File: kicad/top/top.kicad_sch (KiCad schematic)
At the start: 32 parts, among them J1 OLED_128x64, J2 Conn_01x15, SW1 SW_SPDT, SW2 RotaryEncoder_Switch

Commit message: added bottom part of pcb, added 3d model for adafruit feather v2
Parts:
- removed H1, H2, H3, H4: MountingHole, MountingHole:MountingHole_2.2mm_M2, symbol Mechanical:MountingHole
- added H1, H2, H3, H4: MountingHole_Pad, MountingHole:MountingHole_2.2mm_M2_DIN965_Pad, symbol Mechanical:MountingHole_Pad
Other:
- note added: "Top Board"

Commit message: on bottom pcb moved signal connections from back copper to front, left most back copper as ground plane. aligned pins and pin sockets on top and bottom pcb, centered them.
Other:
- note added: "62 mm board 35.5 mm pins"
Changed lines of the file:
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@@
+		)
+	)
+	(text "62 mm board\n35.5 mm pins"
+		(exclude_from_sim no)
+		(at 218.44 110.236 0)
+		(effects
+			(font
+				(size 1.27 1.27)
+			)
 		)
 	)

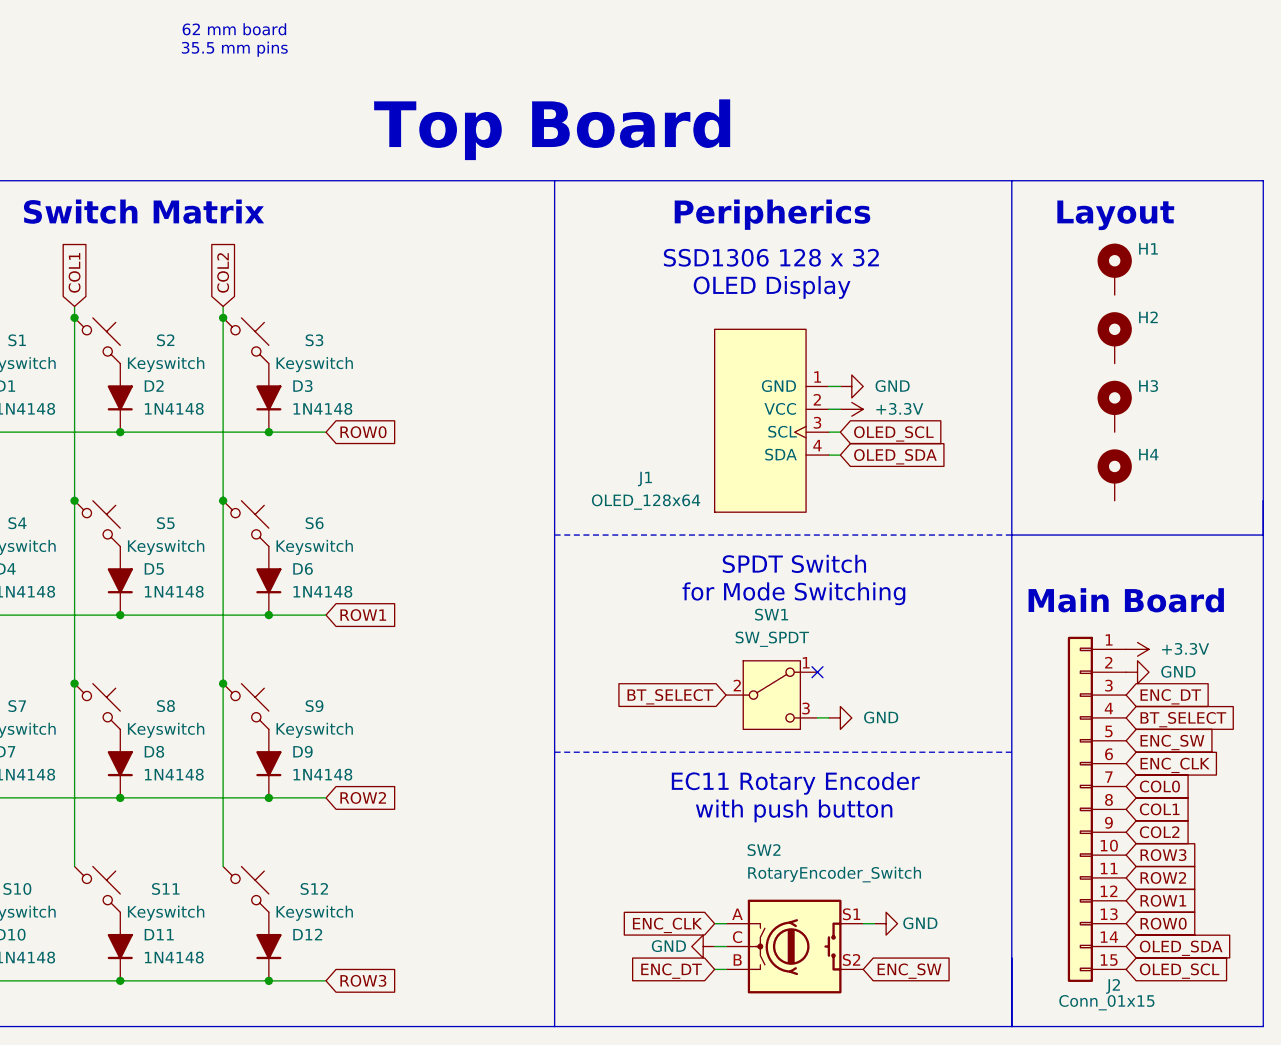
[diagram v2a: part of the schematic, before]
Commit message: modify paths and file locations for portability, added mounting pins to encoder, changed symbol, footprint and 3d of switch to correlate to what im using
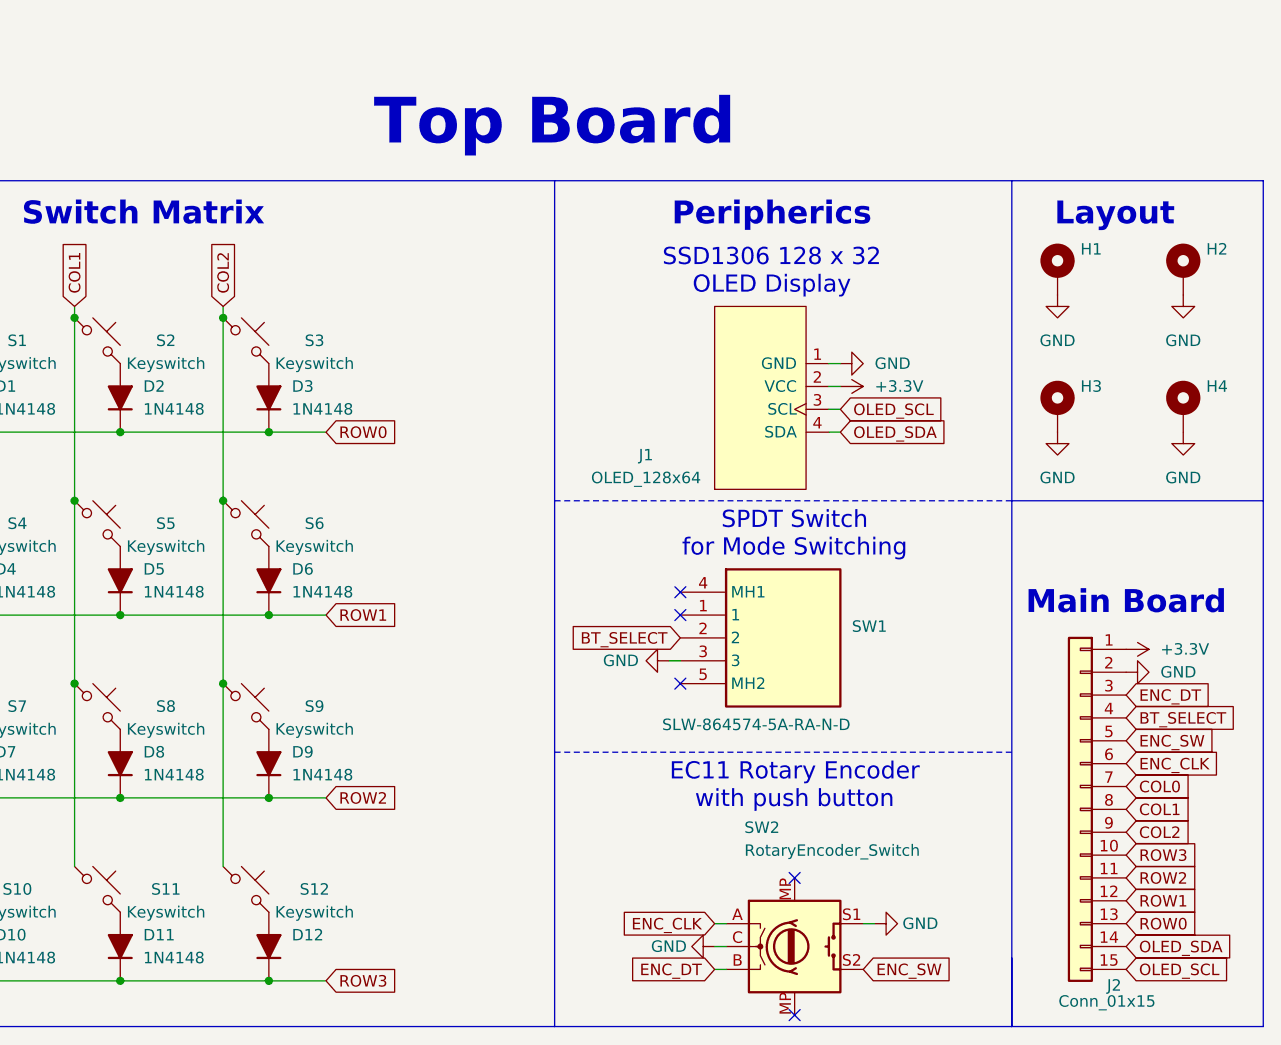
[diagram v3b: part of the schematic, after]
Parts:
- removed SW1: SW_SPDT, Button_Switch_THT:SW_Slide_SPDT_Angled_CK_OS102011MA1Q, symbol Switch:SW_SPDT
- added SW1: SLW-864574-5A-RA-N-D, Project-Footprints:SLW8645745ARAND, symbol Top-Library:SLW-864574-5A-RA-N-D
- D1, D10, D11, D12, D2, D3, D4, D5, D6, D7, D8, D9: footprint Diode_THT:D_DO-35_SOD27_P7.62mm_Horizontal -> Project-Footprints:D_DO-35_SOD27_P7.62mm_Horizontal; symbol PCM_Diode_AKL:1N4148 -> Top-Library:1N4148
- H1, H2, H3, H4: footprint MountingHole:MountingHole_2.2mm_M2_DIN965_Pad -> Project-Footprints:MountingHole_2.2mm_M2_DIN965_Pad; symbol Mechanical:MountingHole_Pad -> Top-Library:MountingHole_Pad
- J1: footprint ScottoKeebs_Components:OLED_128x64 -> Project-Footprints:OLED_128x64; symbol ScottoKeebs:OLED_128x64 -> Top-Library:OLED_128x64
- J2: footprint Connector_PinHeader_2.54mm:PinHeader_1x15_P2.54mm_Vertical -> Project-Footprints:PinHeader_1x15_P2.54mm_Vertical; symbol Connector_Generic:Conn_01x15 -> Top-Library:Conn_01x15
- S1, S10, S11, S12, S2, S3, S4, S5, S6, S7, S8, S9: footprint ScottoKeebs_Scotto:MX_Hotswap_1.00u -> Project-Footprints:MX_Hotswap_1.00u; symbol ScottoKeebs:Placeholder_Keyswitch -> Top-Library:Placeholder_Keyswitch
- SW2: footprint ScottoKeebs_Scotto:Encoder_EC11_MX -> Project-Footprints:Encoder_EC11_MX; symbol Device:RotaryEncoder_Switch -> Top-Library:RotaryEncoder_Switch
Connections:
- net BT_SELECT: now also SW1.2
- net GND: now also H1.1, H2.1, H3.1, H4.1, SW1.3
- no-connect marks 1 -> 5
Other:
- note removed: "62 mm board 35.5 mm pins"
- moved on the sheet: H1, H2, H3, H4, J1

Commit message: finalised mounting hole and pins position, changed gpios
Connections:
- net +3.3V: now also SW1.1
- net COL0: now also J2.11 (Pin_11); no longer J2.7 (Pin_7)
- net COL1: now also J2.12 (Pin_12); no longer J2.8 (Pin_8)
- net COL2: now also J2.13 (Pin_13); no longer J2.9 (Pin_9)
- net ENC_CLK: now also J2.8 (Pin_8); no longer J2.6 (Pin_6)
- net ENC_DT: now also J2.9 (Pin_9); no longer J2.3 (Pin_3)
- net ENC_SW: now also J2.10 (Pin_10); no longer J2.5 (Pin_5)
- net GND: now also SW1.4 (MH1), SW1.5 (MH2), SW2.MP
- net OLED_SCL: now also J2.14 (Pin_14); no longer J2.15 (Pin_15)
- net OLED_SDA: now also J2.15 (Pin_15); no longer J2.14 (Pin_14)
- net ROW0: now also J2.7 (Pin_7); no longer J2.13 (Pin_13)
- net ROW1: now also J2.6 (Pin_6); no longer J2.12 (Pin_12)
- net ROW2: now also J2.5 (Pin_5); no longer J2.11 (Pin_11)
- net ROW3: now also J2.3 (Pin_3); no longer J2.10 (Pin_10)
- no-connect marks 5 -> 0
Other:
- moved on the sheet: D1, D10, D11, D12, D2, D3, D4, D5, D6, D7, D8, D9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

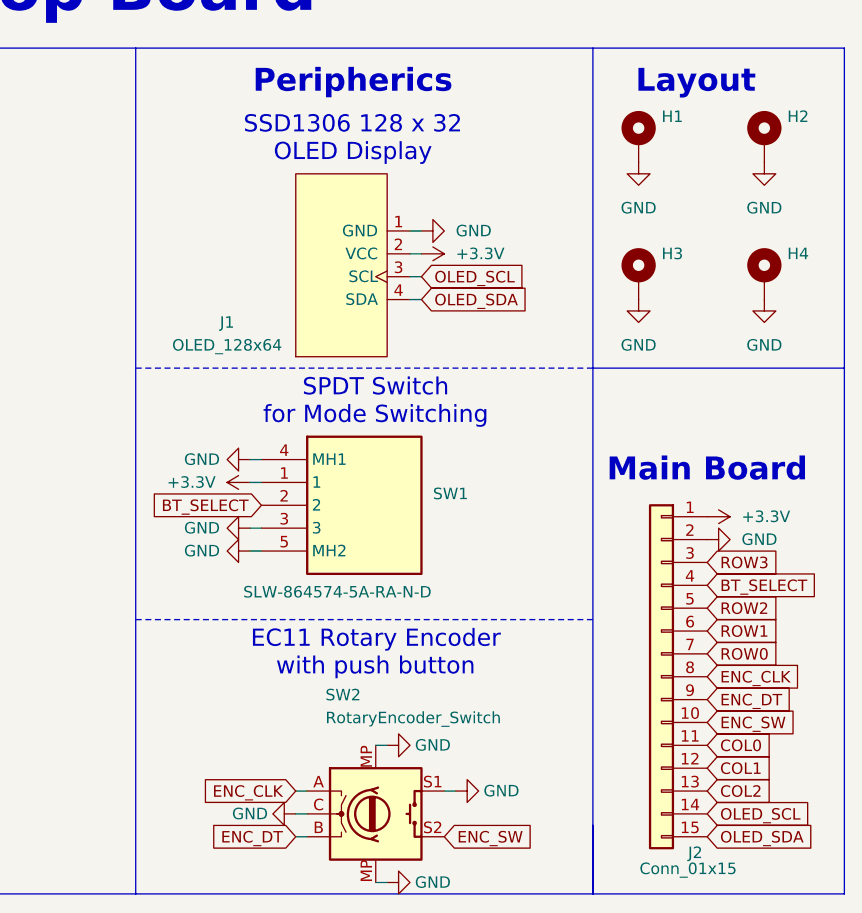
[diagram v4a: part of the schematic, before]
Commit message: Changed from Adafruit Feather V2 to UnkownMaker ProS3 [D] for USB HID feature. Changed OLED from 128x64 to 128x32
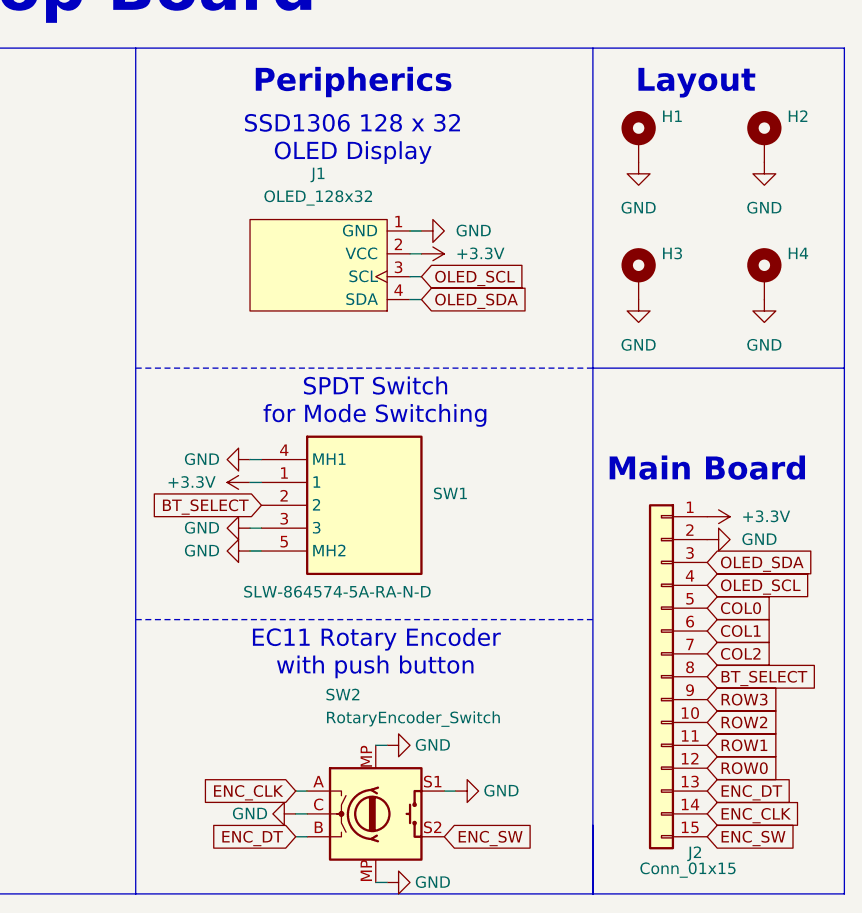
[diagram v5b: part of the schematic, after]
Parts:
- removed J1: OLED_128x64, Project-Footprints:OLED_128x64, symbol Top-Library:OLED_128x64
- added J1: OLED_128x32, ScottoKeebs_Components:OLED_128x32, symbol ScottoKeebs:OLED_128x32
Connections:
- net +3.3V: now also J1.2 (VCC)
- net BT_SELECT: now also J2.8 (Pin_8); no longer J2.4 (Pin_4)
- net COL0: now also J2.5 (Pin_5); no longer J2.11 (Pin_11)
- net COL1: now also J2.6 (Pin_6); no longer J2.12 (Pin_12)
- net COL2: now also J2.7 (Pin_7); no longer J2.13 (Pin_13)
- net ENC_CLK: now also J2.14 (Pin_14); no longer J2.8 (Pin_8)
- net ENC_DT: now also J2.13 (Pin_13); no longer J2.9 (Pin_9)
- net ENC_SW: now also J2.15 (Pin_15); no longer J2.10 (Pin_10)
- net GND: now also J1.1 (GND)
- net OLED_SCL: now also J2.4 (Pin_4), J1.3 (SCL); no longer J2.14 (Pin_14)
- net OLED_SDA: now also J2.3 (Pin_3), J1.4 (SDA); no longer J2.15 (Pin_15)
- net ROW0: now also J2.12 (Pin_12); no longer J2.7 (Pin_7)
- net ROW1: now also J2.11 (Pin_11); no longer J2.6 (Pin_6)
- net ROW2: now also J2.10 (Pin_10); no longer J2.5 (Pin_5)
- net ROW3: now also J2.9 (Pin_9); no longer J2.3 (Pin_3)
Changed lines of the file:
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@@
 	(global_label "ROW0"
 		(shape input)
-		(at 208.28 109.22 0)
+		(at 208.28 121.92 0)
 		(fields_autoplaced yes)
 		(effects
@@
 		)
 		(property "Intersheetrefs" "${INTERSHEET_REFS}"
-			(at 216.5266 109.22 0)
+			(at 216.5266 121.92 0)
 			(effects
 				(font
@@
 	(global_label "OLED_SDA"
 		(shape input)
-		(at 208.28 129.54 0)
+		(at 208.28 99.06 0)
 		(fields_autoplaced yes)
 		(effects
@@
 		)
 		(property "Intersheetrefs" "${INTERSHEET_REFS}"
-			(at 220.5785 129.54 0)
+			(at 220.5785 99.06 0)
 			(effects
 				(font
@@
 	(global_label "ENC_DT"
 		(shape input)
-		(at 208.28 114.3 0)
+		(at 208.28 124.46 0)
 		(fields_autoplaced yes)
 		(effects
@@
 		)
 		(property "Intersheetrefs" "${INTERSHEET_REFS}"
-			(at 218.2199 114.3 0)
+			(at 218.2199 124.46 0)
 			(effects
 				(font
@@
 	(global_label "COL0"
 		(shape input)
-		(at 208.28 119.38 0)
+		(at 208.28 104.14 0)
 		(fields_autoplaced yes)
 		(effects
@@
 		)
 		(property "Intersheetrefs" "${INTERSHEET_REFS}"
-			(at 216.1033 119.38 0)
+			(at 216.1033 104.14 0)
 			(effects
 				(font
@@
 	(global_label "BT_SELECT"
 		(shape input)
-		(at 208.28 101.6 0)
+		(at 208.28 111.76 0)
 		(fields_autoplaced yes)
 		(effects
@@
 		)
 		(property "Intersheetrefs" "${INTERSHEET_REFS}"
-			(at 221.2436 101.6 0)
+			(at 221.2436 111.76 0)
 			(effects
 				(font
@@
 	(global_label "OLED_SCL"
 		(shape input)
-		(at 208.28 127 0)
+		(at 208.28 101.6 0)
 		(fields_autoplaced yes)
 		(effects
@@
 		)
 		(property "Intersheetrefs" "${INTERSHEET_REFS}"
-			(at 220.518 127 0)
+			(at 220.518 101.6 0)
 			(effects
 				(font
@@
 	(global_label "ROW1"
 		(shape input)
-		(at 208.28 106.68 0)
+		(at 208.28 119.38 0)
 		(fields_autoplaced yes)
 		(effects
@@
 		)
 		(property "Intersheetrefs" "${INTERSHEET_REFS}"
-			(at 216.5266 106.68 0)
+			(at 216.5266 119.38 0)
 			(effects
 				(font
@@
 	(global_label "COL1"
 		(shape input)
-		(at 208.28 121.92 0)
+		(at 208.28 106.68 0)
 		(fields_autoplaced yes)
 		(effects
@@
 		)
 		(property "Intersheetrefs" "${INTERSHEET_REFS}"
-			(at 216.1033 121.92 0)
+			(at 216.1033 106.68 0)
 			(effects
 				(font
@@
 	(global_label "ENC_CLK"
 		(shape input)
-		(at 208.28 111.76 0)
+		(at 208.28 127 0)
 		(fields_autoplaced yes)
 		(effects
@@
 		)
 		(property "Intersheetrefs" "${INTERSHEET_REFS}"
-			(at 219.5504 111.76 0)
+			(at 219.5504 127 0)
 			(effects
 				(font
@@
 	(global_label "ROW2"
 		(shape input)
-		(at 208.28 104.14 0)
+		(at 208.28 116.84 0)
 		(fields_autoplaced yes)
 		(effects
@@
 		)
 		(property "Intersheetrefs" "${INTERSHEET_REFS}"
-			(at 216.5266 104.14 0)
+			(at 216.5266 116.84 0)
 			(effects
 				(font
@@
 	(global_label "COL2"
 		(shape input)
-		(at 208.28 124.46 0)
+		(at 208.28 109.22 0)
 		(fields_autoplaced yes)
 		(effects
@@
 		)
 		(property "Intersheetrefs" "${INTERSHEET_REFS}"
-			(at 216.1033 124.46 0)
+			(at 216.1033 109.22 0)
 			(effects
 				(font
@@
 	(global_label "ENC_SW"
 		(shape input)
-		(at 208.28 116.84 0)
+		(at 208.28 129.54 0)
 		(fields_autoplaced yes)
 		(effects
@@
 		)
 		(property "Intersheetrefs" "${INTERSHEET_REFS}"
-			(at 218.6432 116.84 0)
+			(at 218.6432 129.54 0)
 			(effects
 				(font
@@
 	(global_label "ROW3"
 		(shape input)
-		(at 208.28 99.06 0)
+		(at 208.28 114.3 0)
 		(fields_autoplaced yes)
 		(effects
@@
 		)
 		(property "Intersheetrefs" "${INTERSHEET_REFS}"
-			(at 216.5266 99.06 0)
+			(at 216.5266 114.3 0)
 			(effects
 				(font
@@
 	)
 	(symbol
+		(lib_id "ScottoKeebs:OLED_128x32")
+		(at 172.72 66.04 180)
+		(unit 1)
+		(exclude_from_sim no)
+		(in_bom yes)
+		(on_board yes)
+		(dnp no)
+		(fields_autoplaced yes)
+		(property "Reference" "J1"
+			(at 165.1 55.88 0)
+			(effects
+				(font
+					(size 1.27 1.27)
+				)
+			)
+		)
+		(property "Value" "OLED_128x32"
+			(at 165.1 58.42 0)
+			(effects
+				(font
+					(size 1.27 1.27)
+				)
+			)
+		)
+		(property "Footprint" "ScottoKeebs_Components:OLED_128x32"
+			(at 172.72 74.93 0)
+			(effects
+				(font
+					(size 1.27 1.27)
+				)
+				(hide yes)
+			)
+		)
+		(property "Datasheet" ""
+			(at 172.72 67.31 0)
+			(effects
+				(font
+					(size 1.27 1.27)
+				)
+				(hide yes)
+			)
+		)
+		(property "Description" ""
+			(at 172.72 66.04 0)
+			(effects
+				(font
+					(size 1.27 1.27)
+				)
+				(hide yes)
+			)
+		)
+		(pin "3"
+		)
+		(pin "2"
+		)
+		(pin "1"
+		)
+		(pin "4"
+		)
+		(instances
+			(project ""
+				(path "/ca9ba2d9-89c9-46e3-92f6-4a1ef1b0894f"
+					(reference "J1")
+					(unit 1)
+				)
+			)
+		)
+	)
+	(symbol
 		(lib_id "Top-Library:Placeholder_Keyswitch")
 		(at 110.49 100.33 0)
@@
 					(unit 1)
 				)
-			)
-		)
-	)
-	(symbol
-		(lib_id "Top-Library:OLED_128x64")
-		(at 172.72 66.04 270)
-		(unit 1)
-		(exclude_from_sim no)
-		(in_bom yes)
-		(on_board yes)
-		(dnp no)
-		(property "Reference" "J1"
-			(at 154.94 72.39 90)
-			(effects
-				(font
-					(size 1.27 1.27)
-				)
-			)
-		)
-		(property "Value" "OLED_128x64"
-			(at 154.94 74.93 90)
-			(effects
-				(font
-					(size 1.27 1.27)
-				)
-			)
-		)
-		(property "Footprint" "Project-Footprints:OLED_128x64"
-			(at 158.75 66.04 0)
-			(effects
-				(font
-					(size 1.27 1.27)
-				)
-				(hide yes)
-			)
-		)
-		(property "Datasheet" ""
-			(at 172.72 67.31 90)
-			(effects
-				(font
-					(size 1.27 1.27)
-				)
-				(hide yes)
-			)
-		)
-		(property "Description" ""
-			(at 172.72 66.04 0)
-			(effects
-				(font
-					(size 1.27 1.27)
-				)
-				(hide yes)
-			)
-		)
-		(pin "1"
-		)
-		(pin "4"
-		)
-		(pin "3"
-		)
-		(pin "2"
-		)
-		(instances
-			(project ""
-				(path "/ca9ba2d9-89c9-46e3-92f6-4a1ef1b0894f"
-					(reference "J1")
-					(unit 1)
-				)
